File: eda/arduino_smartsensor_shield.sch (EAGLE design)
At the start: 9 parts, among them J1 ARDUINO_R3_SHIELD

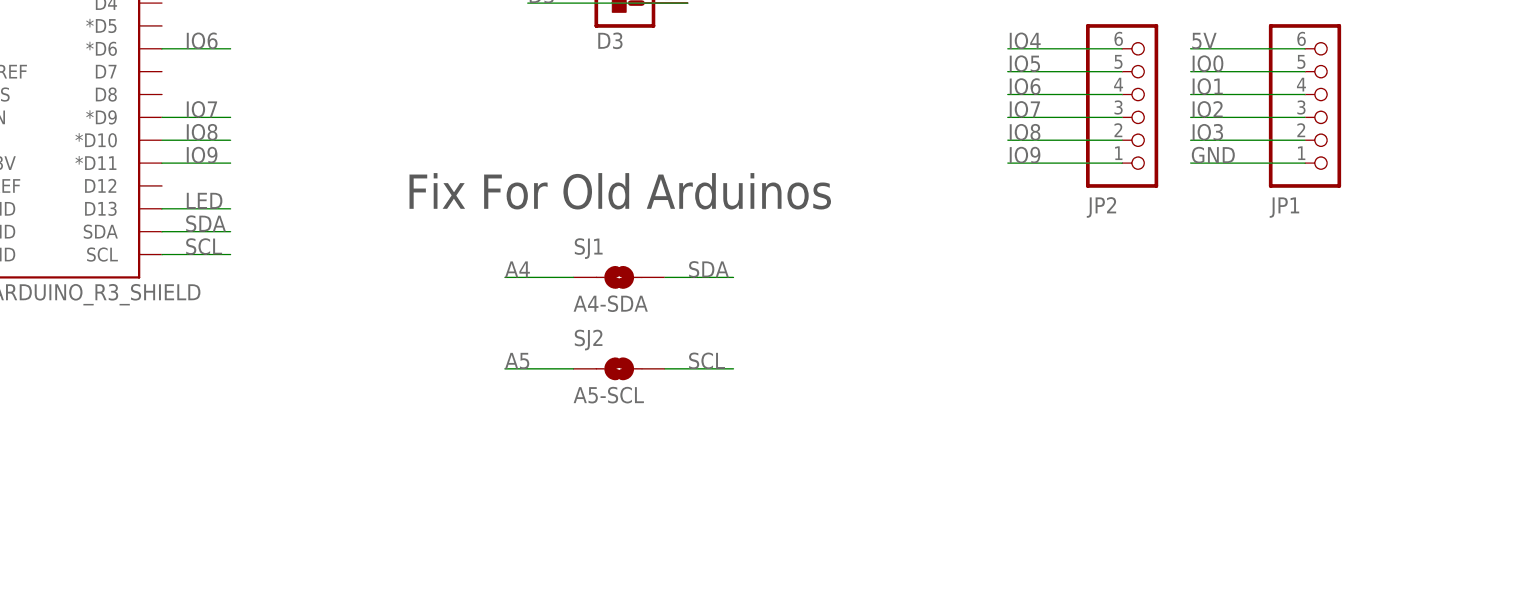
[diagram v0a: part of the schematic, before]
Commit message: Add ISP connector to Arduino smart device shield
to optionally program smart device using Arduino as ISP
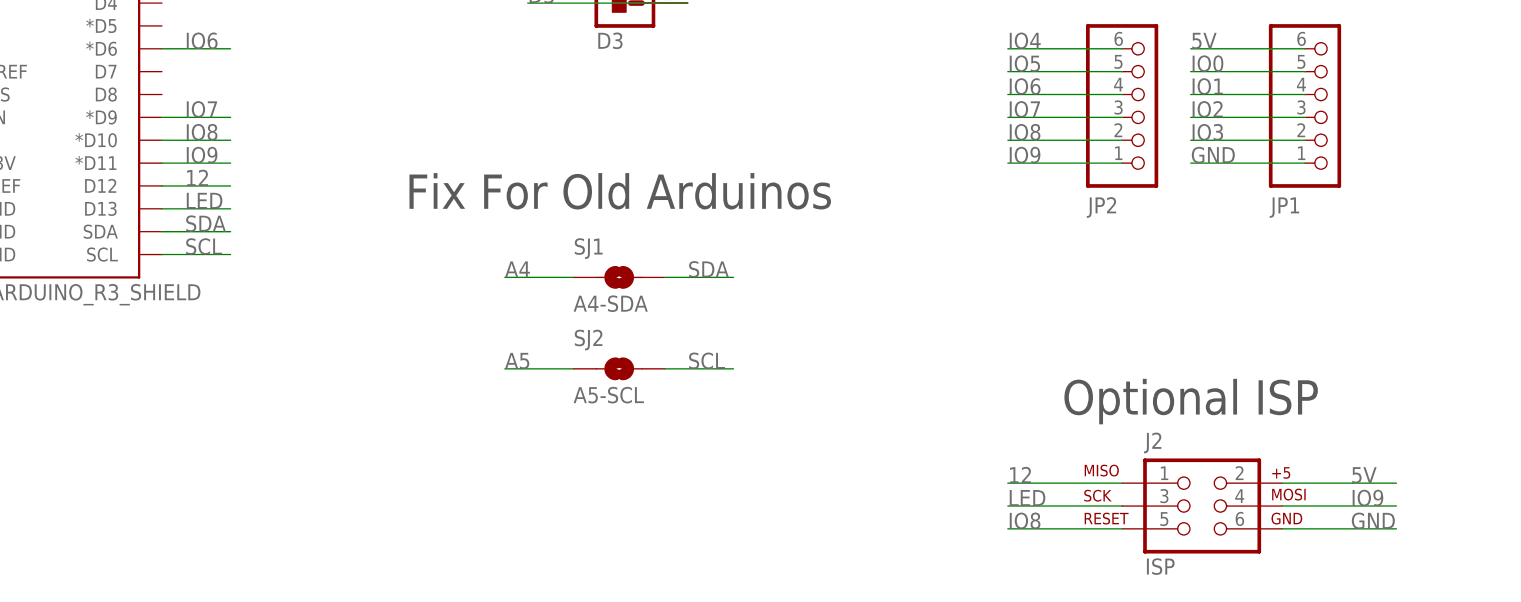
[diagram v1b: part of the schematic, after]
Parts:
- added J2: ISP, pie:AVR_SPI_PRG_6PTH
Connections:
- new net 12: J1.D12, J2.1
- net 5V: now also J2.2
- net GND: now also J2.6
- net IO8: now also J2.5
- net IO9: now also J2.4
- net LED: now also J2.3
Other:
- note added: "Optional ISP"
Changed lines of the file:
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@@
 <setting verticaltext="up"/>
 </settings>
-<grid distance="0.1" unitdist="inch" unit="inch" style="lines" multiple="1" display="yes" altdistance="0.01" altunitdist="inch" altunit="inch"/>
+<grid distance="0.1" unitdist="inch" unit="inch" style="lines" multiple="1" display="no" altdistance="0.01" altunitdist="inch" altunit="inch"/>
 <layers>
 <layer number="1" name="Top" color="4" fill="1" visible="yes" active="no"/>
@@
 <part name="JP1" library="pie" deviceset="PINHD-1X6" device="STRAIN-RELIEF"/>
 <part name="JP2" library="pie" deviceset="PINHD-1X6" device=""/>
+<part name="J2" library="pie" deviceset="AVR_SPI_PRG_6" device="PTH" value="ISP"/>
 </parts>
 <sheets>
@@
 <text x="180.34" y="109.22" size="3.81" layer="97" font="vector" ratio="15" align="bottom-center">Smart Device Connector</text>
 <text x="182.88" y="157.48" size="3.81" layer="97" font="vector" ratio="15" align="bottom-center">Status Light</text>
+<text x="182.88" y="58.42" size="3.81" layer="97" font="vector" ratio="15" align="bottom-center">Optional ISP</text>
 </plain>
 <instances>
@@
 <instance part="JP1" gate="A" x="195.58" y="92.71" rot="MR180"/>
 <instance part="JP2" gate="A" x="175.26" y="92.71" rot="MR180"/>
+<instance part="J2" gate="G$1" x="182.88" y="48.26"/>
 </instances>
 <busses>
@@
 <label x="35.56" y="76.2" size="1.778" layer="95"/>
 </segment>
+<segment>
+<pinref part="J2" gate="G$1" pin="6"/>
+<wire x1="205.74" y1="45.72" x2="193.04" y2="45.72" width="0.1524" layer="91"/>
+<label x="200.66" y="45.72" size="1.778" layer="95"/>
+</segment>
 </net>
 <net name="5V" class="0">
@@
 <label x="35.56" y="88.9" size="1.778" layer="95"/>
 </segment>
+<segment>
+<pinref part="J2" gate="G$1" pin="2"/>
+<wire x1="205.74" y1="50.8" x2="193.04" y2="50.8" width="0.1524" layer="91"/>
+<label x="200.66" y="50.8" size="1.778" layer="95"/>
+</segment>
 </net>
 <net name="N$1" class="0">
@@
 <label x="71.12" y="86.36" size="1.778" layer="95"/>
 </segment>
+<segment>
+<pinref part="J2" gate="G$1" pin="4"/>
+<wire x1="205.74" y1="48.26" x2="193.04" y2="48.26" width="0.1524" layer="91"/>
+<label x="200.66" y="48.26" size="1.778" layer="95"/>
+</segment>
 </net>
 <net name="IO4" class="0">
@@
 <label x="71.12" y="88.9" size="1.778" layer="95"/>
 </segment>
+<segment>
+<pinref part="J2" gate="G$1" pin="5"/>
+<wire x1="162.56" y1="45.72" x2="175.26" y2="45.72" width="0.1524" layer="91"/>
+<label x="162.56" y="45.72" size="1.778" layer="95"/>
+</segment>
 </net>
 <net name="D2" class="0">
@@
 <label x="71.12" y="81.28" size="1.778" layer="95"/>
 </segment>
-</net>
+<segment>
+<pinref part="J2" gate="G$1" pin="3"/>
+<wire x1="162.56" y1="48.26" x2="175.26" y2="48.26" width="0.1524" layer="91"/>
+<label x="162.56" y="48.26" size="1.778" layer="95"/>
+</segment>
+</net>
+<net name="12" class="0">
+<segment>
+<pinref part="J2" gate="G$1" pin="1"/>
+<wire x1="175.26" y1="50.8" x2="162.56" y2="50.8" width="0.1524" layer="91"/>
+<label x="162.56" y="50.8" size="1.778" layer="95"/>
+</segment>
+<segment>
+<pinref part="J1" gate="G$1" pin="D12"/>
+<wire x1="68.58" y1="83.82" x2="76.2" y2="83.82" width="0.1524" layer="91"/>
+<label x="71.12" y="83.82" size="1.778" layer="95"/>
+</segment>
+</net>

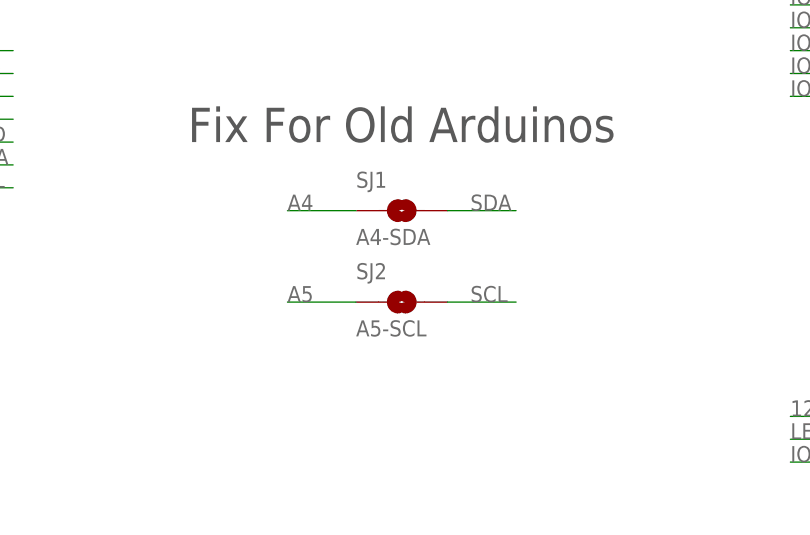
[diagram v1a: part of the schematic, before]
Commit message: SS Arduino shield: added mounting holes, fixed silkscreen, fixed ISP orientation
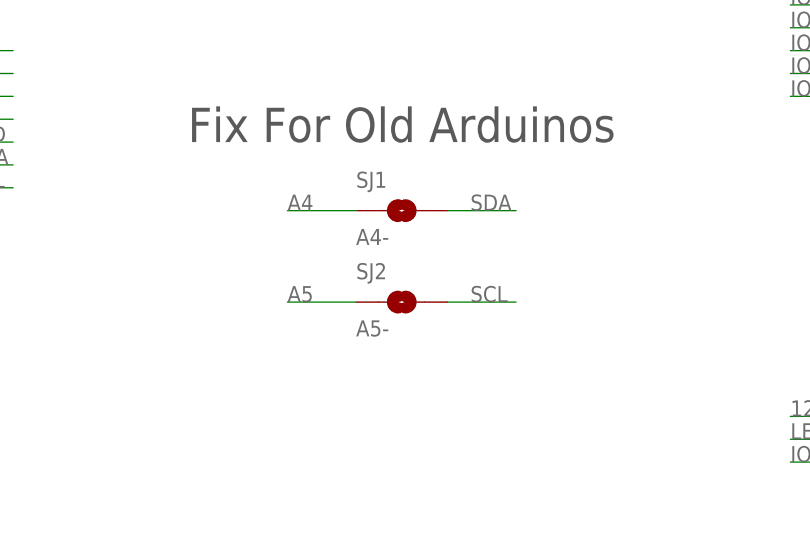
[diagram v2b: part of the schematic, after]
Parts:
- SJ1: value A4-SDA -> A4-
- SJ2: value A5-SCL -> A5-
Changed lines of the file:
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@@
 <grid distance="0.1" unitdist="inch" unit="inch" style="lines" multiple="1" display="no" altdistance="0.01" altunitdist="inch" altunit="inch"/>
 <layers>
-<layer number="1" name="Top" color="4" fill="1" visible="yes" active="no"/>
-<layer number="16" name="Bottom" color="1" fill="1" visible="yes" active="no"/>
-<layer number="17" name="Pads" color="2" fill="1" visible="yes" active="no"/>
-<layer number="18" name="Vias" color="2" fill="1" visible="yes" active="no"/>
-<layer number="19" name="Unrouted" color="6" fill="1" visible="yes" active="no"/>
-<layer number="20" name="Dimension" color="15" fill="1" visible="yes" active="no"/>
-<layer number="21" name="tPlace" color="7" fill="1" visible="yes" active="no"/>
-<layer number="22" name="bPlace" color="7" fill="1" visible="yes" active="no"/>
-<layer number="23" name="tOrigins" color="15" fill="1" visible="yes" active="no"/>
-<layer number="24" name="bOrigins" color="15" fill="1" visible="yes" active="no"/>
-<layer number="25" name="tNames" color="7" fill="1" visible="yes" active="no"/>
-<layer number="26" name="bNames" color="7" fill="1" visible="yes" active="no"/>
-<layer number="27" name="tValues" color="7" fill="1" visible="yes" active="no"/>
-<layer number="28" name="bValues" color="7" fill="1" visible="yes" active="no"/>
+<layer number="1" name="Top" color="4" fill="1" visible="no" active="no"/>
+<layer number="16" name="Bottom" color="1" fill="1" visible="no" active="no"/>
+<layer number="17" name="Pads" color="2" fill="1" visible="no" active="no"/>
+<layer number="18" name="Vias" color="2" fill="1" visible="no" active="no"/>
+<layer number="19" name="Unrouted" color="6" fill="1" visible="no" active="no"/>
+<layer number="20" name="Dimension" color="15" fill="1" visible="no" active="no"/>
+<layer number="21" name="tPlace" color="7" fill="1" visible="no" active="no"/>
+<layer number="22" name="bPlace" color="7" fill="1" visible="no" active="no"/>
+<layer number="23" name="tOrigins" color="15" fill="1" visible="no" active="no"/>
+<layer number="24" name="bOrigins" color="15" fill="1" visible="no" active="no"/>
+<layer number="25" name="tNames" color="7" fill="1" visible="no" active="no"/>
+<layer number="26" name="bNames" color="7" fill="1" visible="no" active="no"/>
+<layer number="27" name="tValues" color="7" fill="1" visible="no" active="no"/>
+<layer number="28" name="bValues" color="7" fill="1" visible="no" active="no"/>
 <layer number="29" name="tStop" color="7" fill="3" visible="no" active="no"/>
 <layer number="30" name="bStop" color="7" fill="6" visible="no" active="no"/>
@@
 <layer number="35" name="tGlue" color="7" fill="4" visible="no" active="no"/>
 <layer number="36" name="bGlue" color="7" fill="5" visible="no" active="no"/>
-<layer number="37" name="tTest" color="7" fill="1" visible="yes" active="no"/>
-<layer number="38" name="bTest" color="7" fill="1" visible="yes" active="no"/>
+<layer number="37" name="tTest" color="7" fill="1" visible="no" active="no"/>
+<layer number="38" name="bTest" color="7" fill="1" visible="no" active="no"/>
 <layer number="39" name="tKeepout" color="4" fill="11" visible="no" active="no"/>
 <layer number="40" name="bKeepout" color="1" fill="11" visible="no" active="no"/>
@@
 <layer number="44" name="Drills" color="7" fill="1" visible="no" active="no"/>
 <layer number="45" name="Holes" color="7" fill="1" visible="no" active="no"/>
-<layer number="46" name="Milling" color="3" fill="1" visible="yes" active="no"/>
-<layer number="47" name="Measures" color="7" fill="1" visible="yes" active="no"/>
-<layer number="48" name="Document" color="7" fill="1" visible="yes" active="no"/>
-<layer number="49" name="Reference" color="7" fill="1" visible="yes" active="no"/>
-<layer number="50" name="dxf" color="7" fill="1" visible="yes" active="no"/>
-<layer number="51" name="tDocu" color="7" fill="1" visible="yes" active="no"/>
-<layer number="52" name="bDocu" color="7" fill="1" visible="yes" active="no"/>
-<layer number="53" name="tGND_GNDA" color="7" fill="9" visible="yes" active="no"/>
-<layer number="54" name="bGND_GNDA" color="1" fill="9" visible="yes" active="no"/>
-<layer number="56" name="wert" color="7" fill="1" visible="yes" active="no"/>
-<layer number="57" name="tCAD" color="7" fill="1" visible="yes" active="no"/>
-<layer number="59" name="tCarbon" color="7" fill="1" visible="yes" active="no"/>
-<layer number="60" name="bCarbon" color="7" fill="1" visible="yes" active="no"/>
+<layer number="46" name="Milling" color="3" fill="1" visible="no" active="no"/>
+<layer number="47" name="Measures" color="7" fill="1" visible="no" active="no"/>
+<layer number="48" name="Document" color="7" fill="1" visible="no" active="no"/>
+<layer number="49" name="Reference" color="7" fill="1" visible="no" active="no"/>
+<layer number="50" name="dxf" color="7" fill="1" visible="no" active="no"/>
+<layer number="51" name="tDocu" color="7" fill="1" visible="no" active="no"/>
+<layer number="52" name="bDocu" color="7" fill="1" visible="no" active="no"/>
+<layer number="53" name="tGND_GNDA" color="7" fill="9" visible="no" active="no"/>
+<layer number="54" name="bGND_GNDA" color="1" fill="9" visible="no" active="no"/>
+<layer number="56" name="wert" color="7" fill="1" visible="no" active="no"/>
+<layer number="57" name="tCAD" color="7" fill="1" visible="no" active="no"/>
+<layer number="59" name="tCarbon" color="7" fill="1" visible="no" active="no"/>
+<layer number="60" name="bCarbon" color="7" fill="1" visible="no" active="no"/>
 <layer number="90" name="Modules" color="5" fill="1" visible="yes" active="yes"/>
 <layer number="91" name="Nets" color="2" fill="1" visible="yes" active="yes"/>
@@
 <part name="JP6" library="pie" deviceset="JMP-OPTION" device="" value="D2"/>
 <part name="JP7" library="pie" deviceset="JMP-OPTION" device="" value="D3"/>
-<part name="SJ1" library="pie" deviceset="SOLDERJUMPER" device="NO" value="A4-SDA"/>
-<part name="SJ2" library="pie" deviceset="SOLDERJUMPER" device="NO" value="A5-SCL"/>
+<part name="SJ1" library="pie" deviceset="SOLDERJUMPER" device="NO" value="A4-"/>
+<part name="SJ2" library="pie" deviceset="SOLDERJUMPER" device="NO" value="A5-"/>
 <part name="JP1" library="pie" deviceset="PINHD-1X6" device="STRAIN-RELIEF"/>
 <part name="JP2" library="pie" deviceset="PINHD-1X6" device=""/>
@@
 </sheet>
 </sheets>
+<errors>
+</errors>
 </schematic>
 </drawing>
